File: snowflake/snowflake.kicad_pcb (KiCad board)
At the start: 2 copper layers, 200.2 x 200.2 mm, 19 parts, among them SW1 SK-12E12-G040, U1 RGB, U2 RGB, U25 TPS61022, U3 RGB, U4 RGB

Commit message: 2/6 branches
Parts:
- added C1: 100nF, Capacitor_SMD:C_0603_1608Metric, F.Cu at (154.4, 124.4)
- added C2: 100nF, Capacitor_SMD:C_0603_1608Metric, F.Cu at (136.0, 95.4)
- added C3: 100nF, Capacitor_SMD:C_0603_1608Metric, F.Cu at (151.6, 68.8)
- added C4: 100nF, Capacitor_SMD:C_0603_1608Metric, F.Cu at (165.5, 98.4)
- added U1: RGB, easyeda2kicad:LED-SMD_4P-L5.0-W5.0-TL_WS2812B-B, F.Cu at (150.0, 123.5)
- added U2: RGB, easyeda2kicad:LED-SMD_4P-L5.0-W5.0-TL_WS2812B-B, F.Cu at (132.0, 95.0)
- added U3: RGB, easyeda2kicad:LED-SMD_4P-L5.0-W5.0-TL_WS2812B-B, F.Cu at (150.0, 65.2)
- added U4: RGB, easyeda2kicad:LED-SMD_4P-L5.0-W5.0-TL_WS2812B-B, F.Cu at (168.0, 95.1)
- moved U7 84.8 mm to (223.4, 107.6), turned to 120 degrees
- moved C7 81.2 mm to (221.1, 110.8), turned to -60 degrees
- moved U6 57.9 mm to (188.6, 106.9), turned to 180 degrees
- moved U8 57.8 mm to (206.6, 138.2), turned to 60 degrees
- moved C6 56.4 mm to (190.3, 110.6), turned to 0 degrees
- moved C8 53.9 mm to (202.5, 137.6), turned to -120 degrees
- moved U5 26.5 mm to (172.9, 136.8), turned to 120 degrees
- moved C5 26.0 mm to (174.4, 141.0), turned to -150 degrees
- moved C26 1.90 mm to (153.8, 168.4)
- moved U25 1.90 mm to (149.9, 168.4)
- moved C25 1.90 mm to (152.3, 168.4)
- moved C27 1.90 mm to (147.1, 167.8)
- moved L1 1.90 mm to (148.2, 164.4)
- moved R1 1.90 mm to (148.8, 170.9)
- moved R2 1.90 mm to (147.7, 170.9)
- renumbered C1 to C5, C2 to C6, C3 to C7, C4 to C8, U1 to U5, U2 to U6, U3 to U7, U4 to U8
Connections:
- U5 pad 4: /DIN -> Net-(U4-DOU)
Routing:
- net +5V: track 156.4 -> 273.7 mm, vias 2 -> 4
- net Net-(U4-DOU): track 0.00 -> 59.9 mm, vias 0 -> 1
- net Net-(U2-DOU): track 0.00 -> 51.9 mm
- net Net-(U3-DOU): track 0.00 -> 50.9 mm
- net Net-(U1-DOU): track 0.00 -> 35.1 mm
- net /BAT+: track 36.2 -> 35.0 mm
- net /EN: track 10.7 -> 11.5 mm

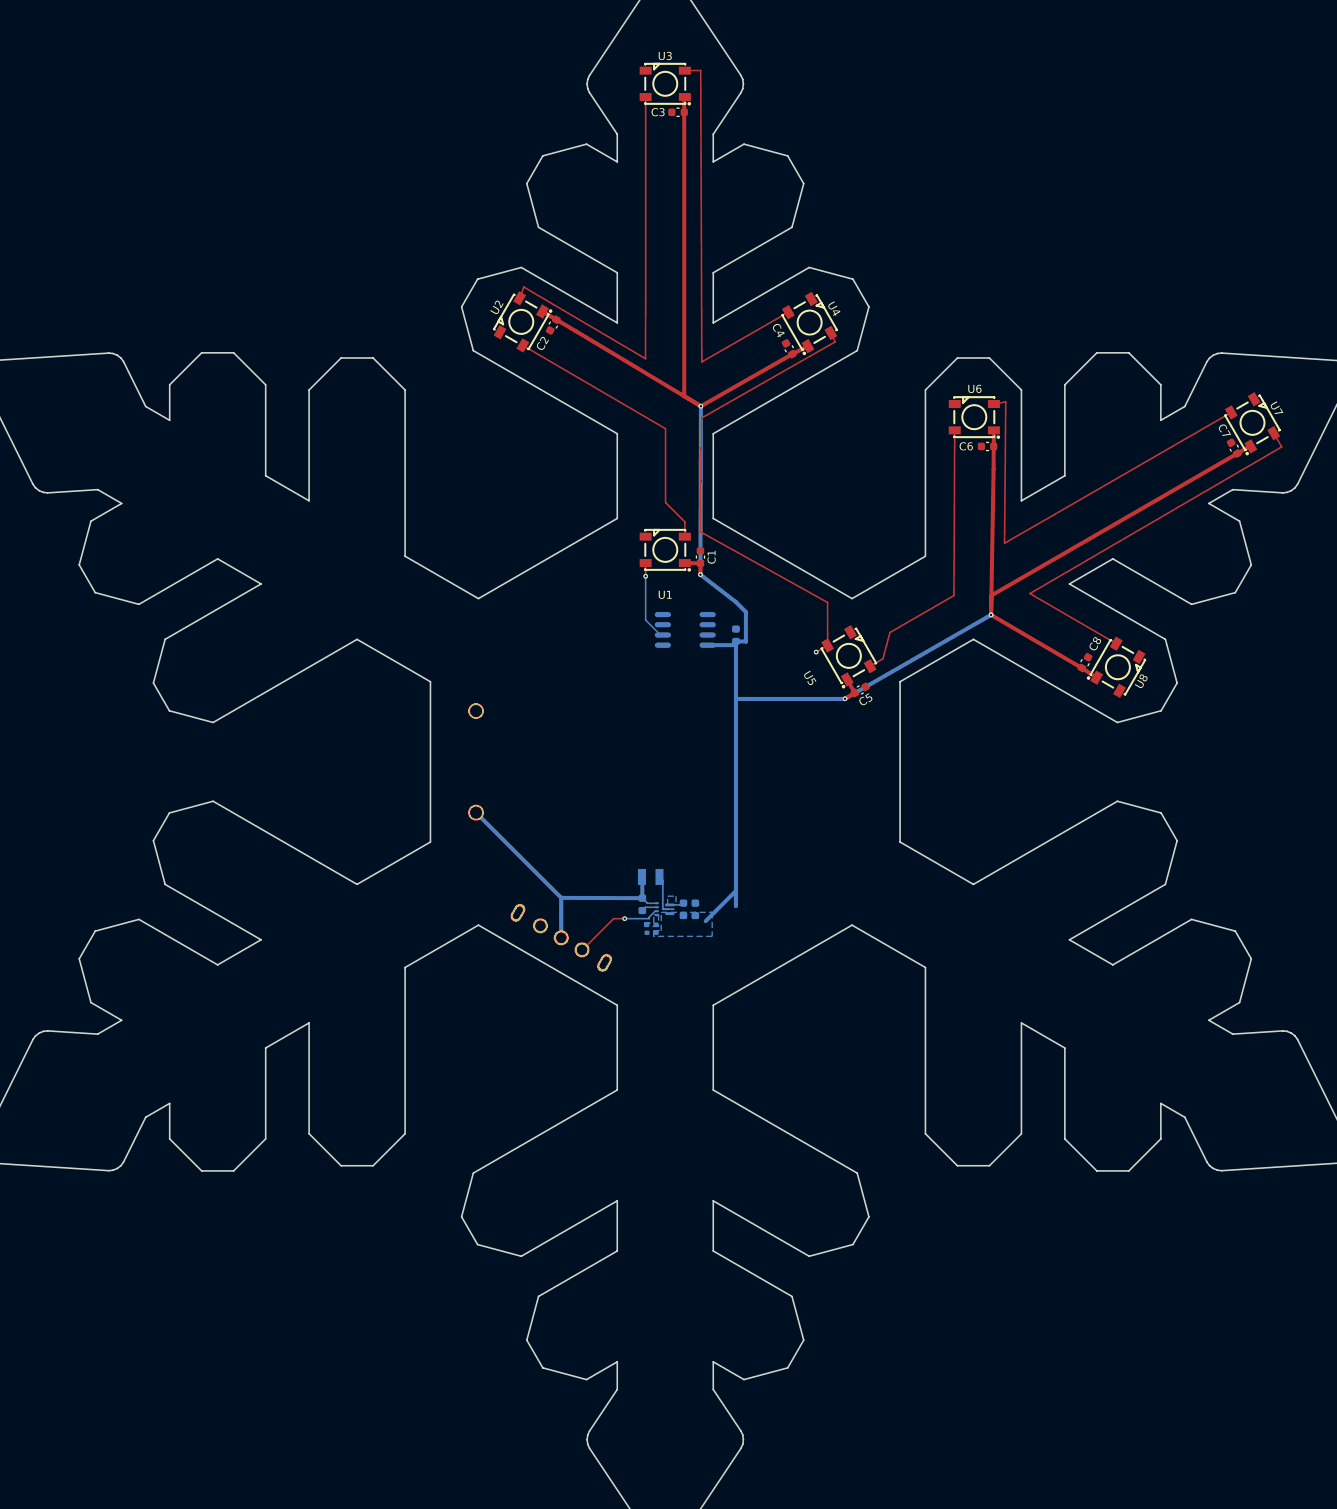
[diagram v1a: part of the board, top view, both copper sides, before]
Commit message: Add JLCPCB Part Numbers
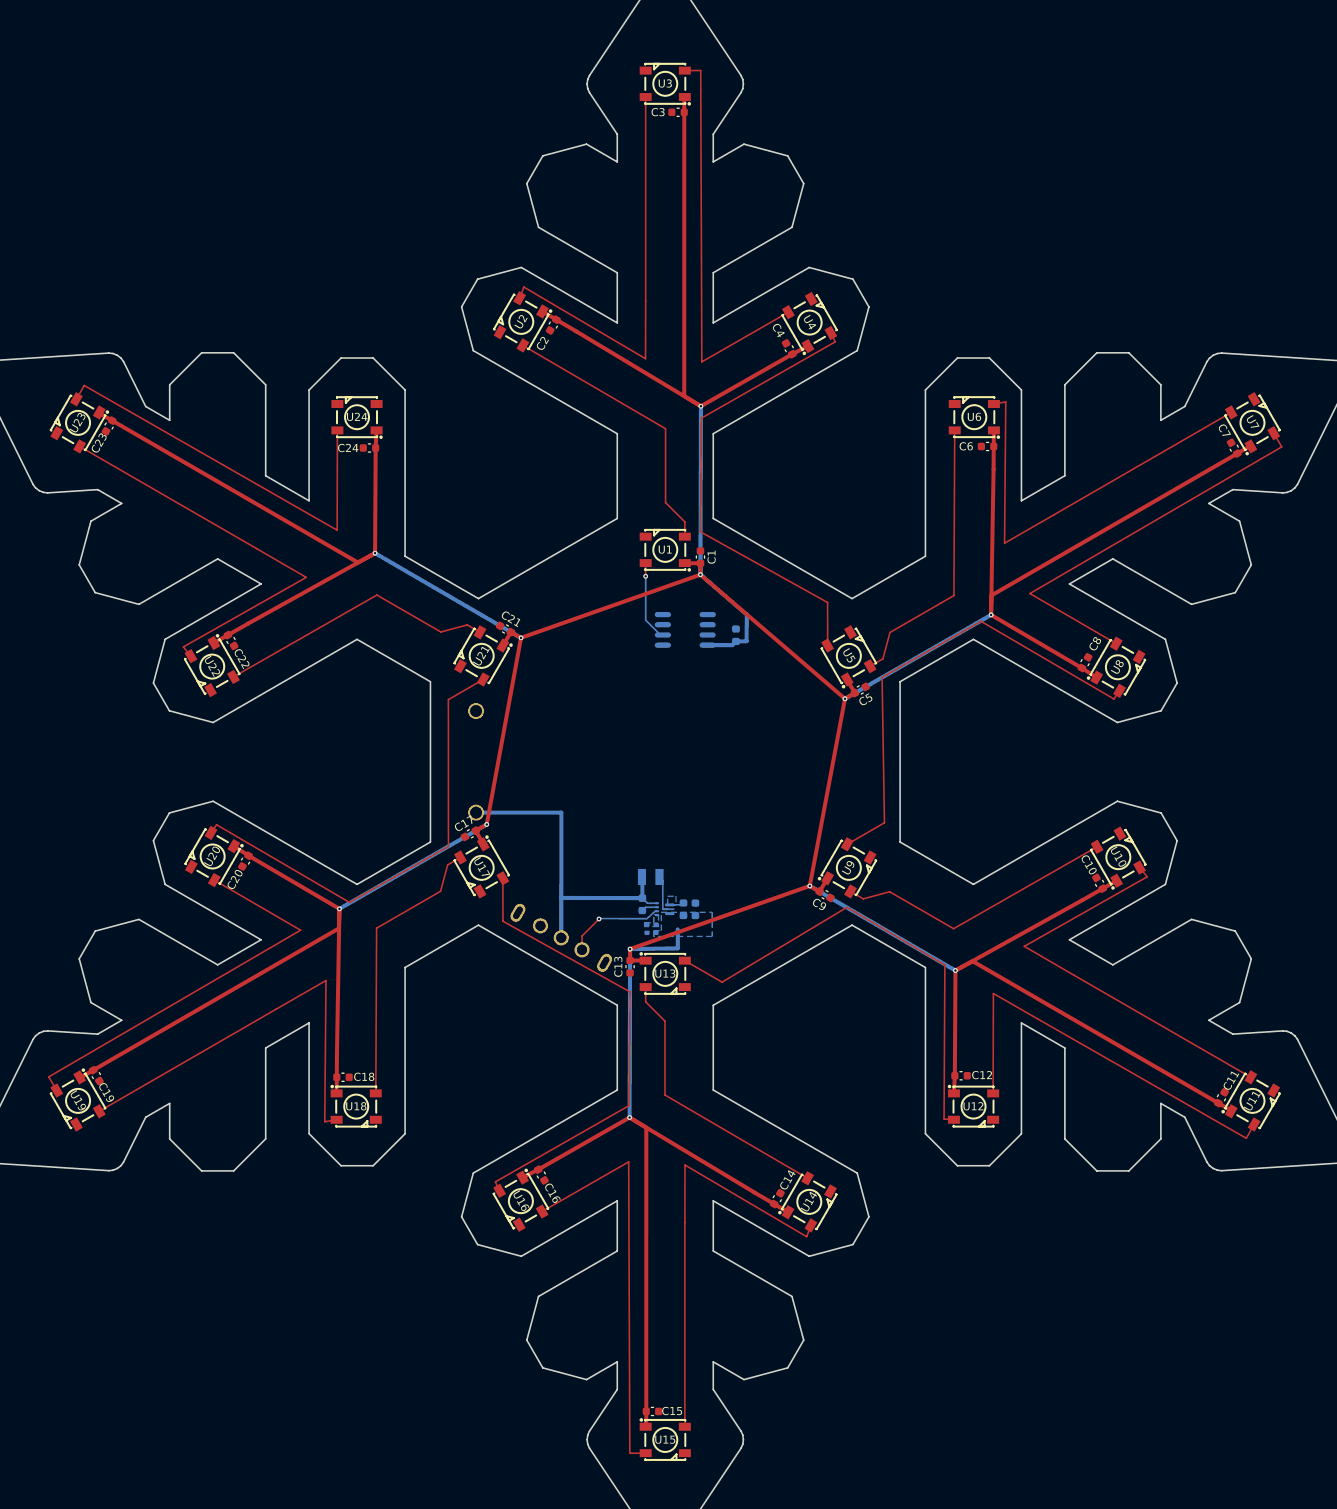
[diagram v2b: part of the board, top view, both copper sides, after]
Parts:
- added C10: 100nF, Capacitor_SMD:C_0603_1608Metric, F.Cu at (204.3, 165.2)
- added C11: 100nF, Capacitor_SMD:C_0603_1608Metric, F.Cu at (219.5, 192.0)
- added C12: 100nF, Capacitor_SMD:C_0603_1608Metric, F.Cu at (187.0, 189.2)
- added C13: 100nF, Capacitor_SMD:C_0603_1608Metric, F.Cu at (145.6, 175.6)
- added C14: 100nF, Capacitor_SMD:C_0603_1608Metric, F.Cu at (164.0, 204.6)
- added C15: 100nF, Capacitor_SMD:C_0603_1608Metric, F.Cu at (148.4, 231.2)
- added C16: 100nF, Capacitor_SMD:C_0603_1608Metric, F.Cu at (134.5, 201.6)
- added C17: 100nF, Capacitor_SMD:C_0603_1608Metric, F.Cu at (125.6, 159.0)
- added C18: 100nF, Capacitor_SMD:C_0603_1608Metric, F.Cu at (109.7, 189.4)
- added C19: 100nF, Capacitor_SMD:C_0603_1608Metric, F.Cu at (78.9, 189.2)
- added C20: 100nF, Capacitor_SMD:C_0603_1608Metric, F.Cu at (97.5, 162.4)
- added C5: 100nF, Capacitor_SMD:C_0603_1608Metric, F.Cu at (174.4, 141.0)
- added C6: 100nF, Capacitor_SMD:C_0603_1608Metric, F.Cu at (190.3, 110.6)
- added C7: 100nF, Capacitor_SMD:C_0603_1608Metric, F.Cu at (221.1, 110.8)
- added C8: 100nF, Capacitor_SMD:C_0603_1608Metric, F.Cu at (202.5, 137.6)
- added C9: 100nF, Capacitor_SMD:C_0603_1608Metric, F.Cu at (170.0, 166.6)
- added U10: TZ-5050S2RGB-5V-I4-H1, easyeda2kicad:LED-SMD_4P-L5.0-W5.0-TL_WS2812B-B, F.Cu at (206.6, 161.9)
- added U11: TZ-5050S2RGB-5V-I4-H1, easyeda2kicad:LED-SMD_4P-L5.0-W5.0-TL_WS2812B-B, F.Cu at (223.4, 192.4)
- added U12: TZ-5050S2RGB-5V-I4-H1, easyeda2kicad:LED-SMD_4P-L5.0-W5.0-TL_WS2812B-B, F.Cu at (188.5, 193.1)
- added U13: TZ-5050S2RGB-5V-I4-H1, easyeda2kicad:LED-SMD_4P-L5.0-W5.0-TL_WS2812B-B, F.Cu at (150.0, 176.5)
- added U14: TZ-5050S2RGB-5V-I4-H1, easyeda2kicad:LED-SMD_4P-L5.0-W5.0-TL_WS2812B-B, F.Cu at (168.0, 205.0)
- added U15: TZ-5050S2RGB-5V-I4-H1, easyeda2kicad:LED-SMD_4P-L5.0-W5.0-TL_WS2812B-B, F.Cu at (150.0, 234.8)
- added U16: TZ-5050S2RGB-5V-I4-H1, easyeda2kicad:LED-SMD_4P-L5.0-W5.0-TL_WS2812B-B, F.Cu at (132.0, 204.9)
- added U17: TZ-5050S2RGB-5V-I4-H1, easyeda2kicad:LED-SMD_4P-L5.0-W5.0-TL_WS2812B-B, F.Cu at (127.1, 163.2)
- added U18: TZ-5050S2RGB-5V-I4-H1, easyeda2kicad:LED-SMD_4P-L5.0-W5.0-TL_WS2812B-B, F.Cu at (111.4, 193.1)
- added U19: TZ-5050S2RGB-5V-I4-H1, easyeda2kicad:LED-SMD_4P-L5.0-W5.0-TL_WS2812B-B, F.Cu at (76.6, 192.4)
- added U20: TZ-5050S2RGB-5V-I4-H1, easyeda2kicad:LED-SMD_4P-L5.0-W5.0-TL_WS2812B-B, F.Cu at (93.4, 161.8)
- added U5: TZ-5050S2RGB-5V-I4-H1, easyeda2kicad:LED-SMD_4P-L5.0-W5.0-TL_WS2812B-B, F.Cu at (172.9, 136.8)
- added U6: TZ-5050S2RGB-5V-I4-H1, easyeda2kicad:LED-SMD_4P-L5.0-W5.0-TL_WS2812B-B, F.Cu at (188.6, 106.9)
- added U7: TZ-5050S2RGB-5V-I4-H1, easyeda2kicad:LED-SMD_4P-L5.0-W5.0-TL_WS2812B-B, F.Cu at (223.4, 107.6)
- added U8: TZ-5050S2RGB-5V-I4-H1, easyeda2kicad:LED-SMD_4P-L5.0-W5.0-TL_WS2812B-B, F.Cu at (206.6, 138.2)
- added U9: TZ-5050S2RGB-5V-I4-H1, easyeda2kicad:LED-SMD_4P-L5.0-W5.0-TL_WS2812B-B, F.Cu at (172.9, 163.2)
- U1, U2, U3, U4: value RGB -> TZ-5050S2RGB-5V-I4-H1
- U21: renamed from U5; value RGB -> TZ-5050S2RGB-5V-I4-H1
- U22: renamed from U6; value RGB -> TZ-5050S2RGB-5V-I4-H1
- U23: renamed from U7; value RGB -> TZ-5050S2RGB-5V-I4-H1
- U24: renamed from U8; value RGB -> TZ-5050S2RGB-5V-I4-H1
- moved U23 146.8 mm to (76.6, 107.6), turned to -120 degrees
- moved C23 140.7 mm to (80.5, 108.0), turned to 60 degrees
- moved U22 100.2 mm to (93.4, 138.1), turned to -60 degrees
- moved U24 100.1 mm to (111.5, 106.9), turned to 180 degrees
- moved C22 97.6 mm to (95.7, 134.8), turned to 120 degrees
- moved C24 93.4 mm to (113.0, 110.8), turned to 0 degrees
- moved U21 45.9 mm to (127.1, 136.8), turned to -120 degrees
- moved C21 45.0 mm to (130.0, 133.4), turned to -30 degrees
- renumbered C5 to C21, C6 to C22, C7 to C23, C8 to C24
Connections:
- U21 pad 4: Net-(U4-DOU) -> Net-(U20-DOU)
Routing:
- net +5V: track 273.7 -> 760.3 mm, vias 4 -> 12
- net Net-(U8-DOU): track 0.00 -> 58.3 mm
- net Net-(U16-DOU): track 0.00 -> 58.3 mm
- net Net-(U12-DOU): track 0.00 -> 58.3 mm
- net Net-(U20-DOU): track 0.00 -> 58.1 mm
- net Net-(U14-DOU): track 0.00 -> 51.9 mm
- net Net-(U6-DOU): track 0.00 -> 51.9 mm
- net Net-(U18-DOU): track 0.00 -> 51.9 mm
- net Net-(U10-DOU): track 0.00 -> 51.9 mm
- net Net-(U19-DOU): track 0.00 -> 50.9 mm
- net Net-(U7-DOU): track 0.00 -> 50.9 mm
- net Net-(U15-DOU): track 0.00 -> 50.9 mm
- net Net-(U11-DOU): track 0.00 -> 50.9 mm
- net Net-(U5-DOU): track 0.00 -> 35.1 mm
- net Net-(U17-DOU): track 0.00 -> 35.1 mm
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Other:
- board text added: "JLCJLCJLCJLC"

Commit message: The nets are happy again
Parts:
- BAT1: value 2468 -> 2462; footprint easyeda2kicad:BAT-TH_2P-L53.0-W24.6-P12.70_2468 -> easyeda2kicad:BAT-TH_2P-P14.50_2462
- C1, C10, C11, C12, C13, C14, C15, C16, C17, C18, C19, C2, C20, C21, C22, C23, C24, C3, C4, C5, C6, C7, C8, C9: moved to B.Cu
- moved BAT1 23.7 mm to (150.0, 150.0)
- moved C23 23.4 mm to (99.9, 121.0), turned to -120 degrees
- moved C11 23.4 mm to (200.1, 178.9), turned to 60 degrees
- moved C3 23.4 mm to (150.0, 92.1), turned to 180 degrees
- moved C15 23.4 mm to (150.0, 207.9), turned to 0 degrees
- moved C19 23.4 mm to (99.9, 178.9), turned to -60 degrees
- moved C7 23.4 mm to (200.1, 121.0), turned to 120 degrees
- moved U3 22.5 mm to (150.0, 87.7), turned to 90 degrees
- moved U15 22.5 mm to (150.0, 212.3), turned to -90 degrees
- moved U7 22.5 mm to (204.0, 118.8), turned to 30 degrees
- moved U19 22.5 mm to (96.0, 181.2), turned to -150 degrees
- moved U11 22.5 mm to (204.0, 181.2), turned to -30 degrees
- moved U23 22.5 mm to (96.0, 118.8), turned to 150 degrees
- moved C17 19.2 mm to (135.1, 175.7), turned to -30 degrees
- moved C5 19.2 mm to (164.9, 124.3), turned to 150 degrees
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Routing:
- net +5V: track 760.3 -> 729.8 mm, vias 12 -> 25
- net Net-(U14-DOU): track 51.9 -> 30.0 mm
- net Net-(U2-DOU): track 51.9 -> 30.0 mm
- net Net-(U6-DOU): track 51.9 -> 30.0 mm
- net Net-(U18-DOU): track 51.9 -> 30.0 mm
- net Net-(U10-DOU): track 51.9 -> 30.0 mm
- net Net-(U22-DOU): track 51.9 -> 30.0 mm
- net Net-(U19-DOU): track 50.9 -> 29.9 mm
- net Net-(U7-DOU): track 50.9 -> 29.9 mm
- net Net-(U23-DOU): track 50.9 -> 29.9 mm
- net Net-(U11-DOU): track 50.9 -> 29.9 mm
- net Net-(U15-DOU): track 50.9 -> 29.9 mm
- net Net-(U3-DOU): track 50.9 -> 29.9 mm
- net Net-(U8-DOU): track 58.3 -> 40.7 mm
- net Net-(U4-DOU): track 58.3 -> 40.7 mm
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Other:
- board size 200.2 x 200.2 mm -> 150.2 x 150.2 mm
- board text removed: "JLCJLCJLCJLC"

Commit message: Use zones instead of traces for +5V
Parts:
- removed C0: 100nF, Capacitor_SMD:C_0603_1608Metric
- removed the C23 at (99.9, 121.0)
- removed MCU1: CH32V003J4M6, easyeda2kicad:SOP-8_L4.9-W3.8-P1.27-LS6.0-BL
- removed the U23 at (96.0, 118.8)
- added C3: 100nF, Capacitor_SMD:C_0603_1608Metric, F.Cu at (149.1, 92.1)
- added C65: 100n, Capacitor_SMD:C_0402_1005Metric, B.Cu at (154.9, 145.3)
- added C66: 100n, Capacitor_SMD:C_0402_1005Metric, B.Cu at (154.9, 146.3)
- added J3: TC2030, Connector:Tag-Connect_TC2030-IDC-NL_2x03_P1.27mm_Vertical, B.Cu at (156.8, 140.7)
- added R3: GT36516, easyeda2kicad:RES-SMD_L3.6-W2.4, F.Cu at (165.1, 155.7)
- added R4: 10k, Resistor_SMD:R_0603_1608Metric, B.Cu at (161.0, 152.4)
- added R5: 560k, Resistor_SMD:R_0603_1608Metric, F.Cu at (146.2, 161.9)
- added R6: 560k, Resistor_SMD:R_0603_1608Metric, F.Cu at (150.2, 161.9)
- added R7: 560k, Resistor_SMD:R_0603_1608Metric, F.Cu at (154.4, 161.7)
- added TP1: PC3, TestPoint:TestPoint_Pad_D2.0mm, B.Cu at (171.4, 150.2)
- added TP2: PC2, TestPoint:TestPoint_Pad_D2.0mm, B.Cu at (167.9, 148.2)
- added TP3: PC1, TestPoint:TestPoint_Pad_D2.0mm, B.Cu at (164.4, 146.2)
- added TP4: PC0, TestPoint:TestPoint_Pad_D2.0mm, B.Cu at (160.9, 144.1)
- added TP5: Touch1, TestPoint:TestPoint_Pad_D2.0mm, F.Cu at (146.2, 158.3)
- added TP6: Touch2, TestPoint:TestPoint_Pad_D2.0mm, F.Cu at (150.2, 158.3)
- added TP7: Touch3, TestPoint:TestPoint_Pad_D2.0mm, F.Cu at (154.3, 158.3)
- added U26: CH32V003F4U6, Package_DFN_QFN:QFN-20-1EP_3x3mm_P0.4mm_EP1.65x1.65mm, B.Cu at (156.9, 148.9)
- added U3: TZ-5050S2RGB-5V-I4-H1, easyeda2kicad:LED-SMD_4P-L5.0-W5.0-TL_WS2812B-B, F.Cu at (150.0, 87.7)
- C1, C10, C11, C12, C13, C14, C15, C16, C17, C18, C19, C2, C20, C21, C22, C24, C4, C5, C6, C7, C8, C9: moved to F.Cu
- C23: renamed from C3; moved to F.Cu
- moved U23 62.3 mm to (96.0, 118.8), turned to 150 degrees
- moved C23 58.6 mm to (99.5, 121.8), turned to -120 degrees
- moved C5 0.92 mm to (164.2, 123.8)
- moved C9 0.92 mm to (179.8, 149.2)
- moved C1 0.92 mm to (134.4, 124.6)
- moved C13 0.92 mm to (165.6, 175.4)
- moved C21 0.92 mm to (120.2, 150.8)
- moved C17 0.92 mm to (135.8, 176.2)
- moved C7 0.85 mm to (199.7, 120.3)
- moved C11 0.85 mm to (200.5, 178.2)
- moved C15 0.85 mm to (150.9, 207.9)
- moved C19 0.85 mm to (100.3, 179.7)
- moved C4 0.74 mm to (158.4, 103.7)
- moved C24 0.74 mm to (114.1, 119.6)
- moved C8 0.74 mm to (194.3, 134.1)
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- renumbered U3 to U23
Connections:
- U23 pad 2: Net-(U3-DOU) -> Net-(U23-DOU)
- U23 pad 4: Net-(U2-DOU) -> Net-(U22-DOU)
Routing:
- net +5V: track 729.8 -> 53.8 mm, vias 25 -> 2
- net GND: track 3.80 -> 61.7 mm, vias 0 -> 48
- net /SWIO: track 0.00 -> 21.8 mm, vias 0 -> 2
- net unconnected-(U24-DOU-Pad2): track 0.00 -> 20.2 mm
- net /RX: track 0.00 -> 15.6 mm, vias 0 -> 2
- net Net-(U26-PC3/T1CH3): track 0.00 -> 14.8 mm
- net /TX: track 0.00 -> 12.3 mm, vias 0 -> 2
- net Net-(U26-PC2/SCL): track 0.00 -> 11.8 mm
- net /DIN: track 20.7 -> 10.2 mm, vias 1 -> 0
- net Net-(U26-PC1/SDA): track 0.00 -> 8.33 mm
- net Net-(U21-DOU): track 44.8 -> 37.2 mm
- net Net-(U20-DOU): track 44.1 -> 37.5 mm
- net Net-(U26-PC0/T2CH3): track 0.00 -> 6.09 mm
- net Net-(U5-DOU): track 43.8 -> 38.6 mm
- net Net-(U1-DOU): track 43.8 -> 38.8 mm
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- added copper zone on F.Cu, net +5V
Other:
- board text added: "JLCJLCJLCJLC"

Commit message: First prototype
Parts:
- removed C65: 100n, Capacitor_SMD:C_0402_1005Metric
- C66: value 100n -> 100nF
- R3: value GT36516 -> C2904881
- U25: footprint Package_DFN_QFN:Texas_RWU0007A_VQFN-7_2x2mm_P0.5mm -> easyeda2kicad:VQFN-7_L2.0-W2.0-P0.55-TL_RWU
- moved U15 62.3 mm to (204.0, 181.2), turned to -30 degrees
- moved U11 62.3 mm to (204.0, 118.9), turned to 30 degrees
- moved U3 62.3 mm to (96.0, 118.8), turned to 150 degrees
- moved U23 62.3 mm to (96.0, 181.1), turned to -150 degrees
- moved U7 62.3 mm to (150.0, 87.7), turned to 90 degrees
- moved U19 62.3 mm to (150.0, 212.3), turned to -90 degrees
- moved C19 57.9 mm to (150.9, 207.9), turned to 0 degrees
- moved C23 57.9 mm to (100.3, 179.7), turned to -60 degrees
- moved C11 57.9 mm to (199.7, 120.3), turned to 120 degrees
- moved C15 57.9 mm to (200.5, 178.2), turned to 60 degrees
- moved C7 57.9 mm to (149.1, 92.1), turned to 180 degrees
- moved C3 57.9 mm to (99.5, 121.8), turned to -120 degrees
- moved TP1 51.9 mm to (122.8, 168.2), turned to -90 degrees
- moved U22 49.4 mm to (114.9, 184.8), turned to -90 degrees
- moved U18 49.4 mm to (162.6, 197.8), turned to -30 degrees
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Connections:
- U26 pad 16: /TOUCH3 -> /TOUCH1
- U26 pad 18: /TOUCH1 -> /TOUCH3
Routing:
- net /TOUCH3: track 0.00 -> 40.8 mm, vias 0 -> 1
- net /TOUCH2: track 0.00 -> 32.6 mm, vias 0 -> 1
- net /TOUCH1: track 0.00 -> 20.8 mm, vias 0 -> 1
- net unconnected-(U24-DOU-Pad2): track 20.2 -> 0.00 mm
- net /LDR_DIV: track 0.00 -> 19.0 mm, vias 0 -> 1
- net /DIN: track 10.2 -> 27.5 mm, vias 0 -> 1
- net Net-(U26-PC0/T2CH3): track 6.09 -> 21.7 mm
- net GND: track 61.7 -> 76.9 mm, vias 48 -> 50
- net Net-(U26-PC1/SDA): track 8.33 -> 20.1 mm
- net /TX: track 12.3 -> 22.4 mm, vias 2 -> 0
- net Net-(U26-PC2/SCL): track 11.8 -> 21.5 mm
- net Net-(U26-PC3/T1CH3): track 14.8 -> 23.0 mm
- net /RX: track 15.6 -> 23.0 mm, vias 2 -> 0
- net +5V: track 53.8 -> 50.9 mm, vias 2 -> 5
- net /BAT+: track 43.7 -> 41.5 mm
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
